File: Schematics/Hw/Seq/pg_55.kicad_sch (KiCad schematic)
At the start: 41 parts, among them U5601 F240, U5602 F00, U5603 F251, U5604 F251, U5605 F04, U5606 F04, U5607 F151, U5608 F04, U5609 F04, U5610 F04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

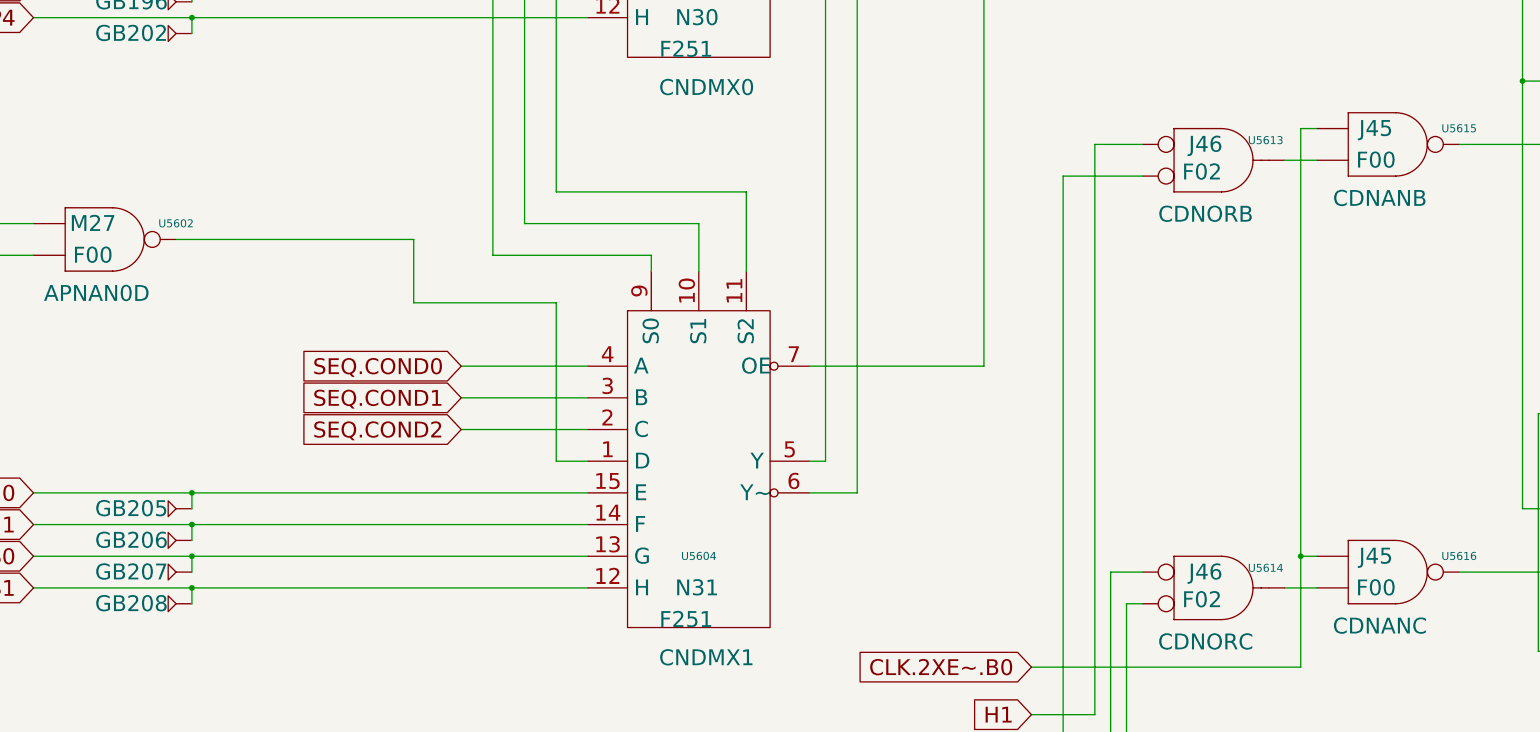
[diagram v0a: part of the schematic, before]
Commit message: Upgrade to KiCad9
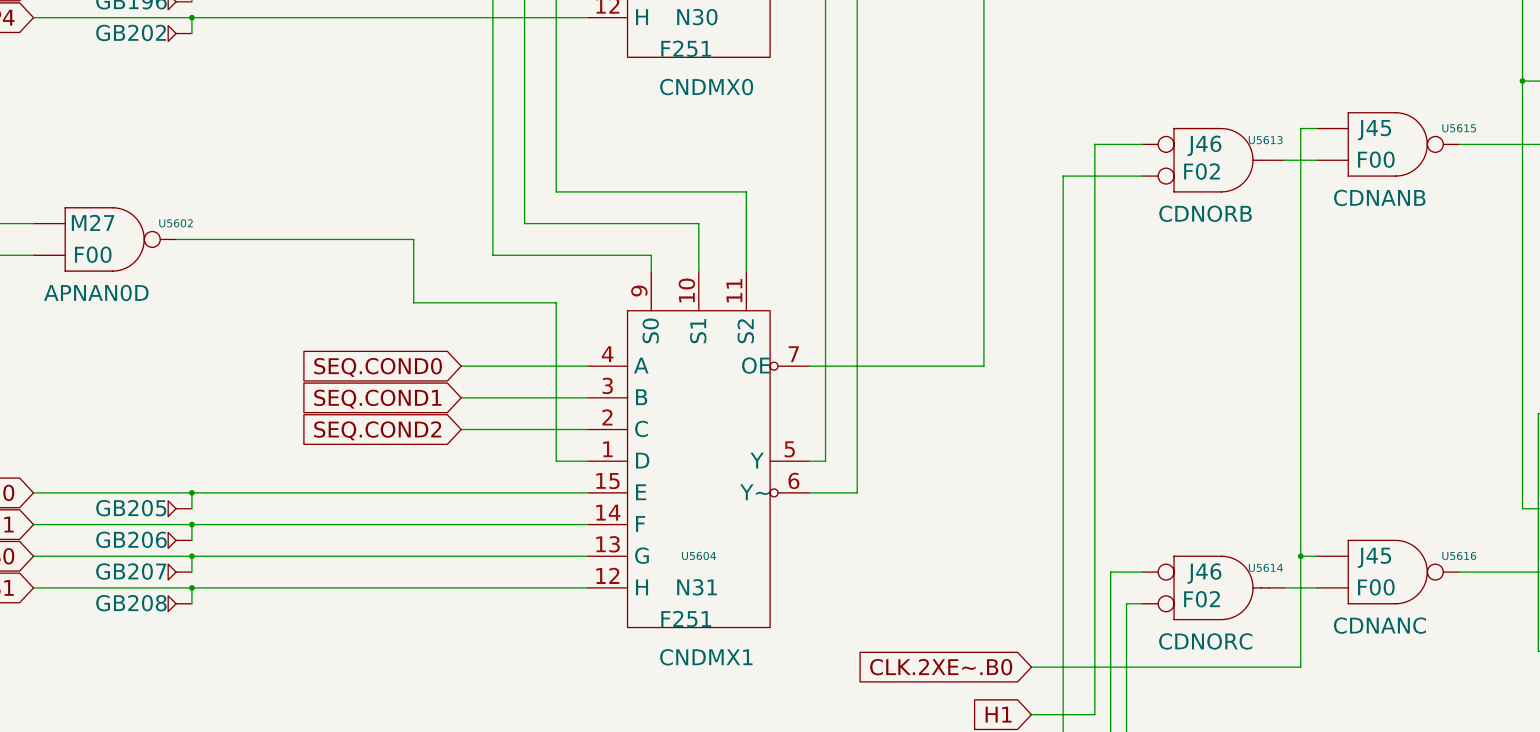
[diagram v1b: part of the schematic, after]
